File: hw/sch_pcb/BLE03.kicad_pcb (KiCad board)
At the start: 2 copper layers, 40 parts, among them J2 3.3-5V, J3 JUMP_5X2, J4 Conn_Coaxial, J5 HEADER_2x06_PARALLEL, M1 HOLE, M2 HOLE, M3 HOLE, M4 HOLE, U2 TXS0104EPW, U3 TXS0104EPW, U4 MIC5504-1.8YM5, U5 TXS0108EPW, U6 LFB212G45CG1C187, Y2 LFSPXO009682

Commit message: Adding connectors and other components
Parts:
- removed C15: 10pF, Capacitor_SMD:C_0603_1608Metric
- removed R4: 2k2, Resistor_SMD:R_0603_1608Metric
- removed R5: 10k, Resistor_SMD:R_0603_1608Metric
- removed U5: TXS0108EPW, Package_SO:TSSOP-20_4.4x6.5mm_P0.65mm
- removed U6: LFB212G45CG1C187, MLAB_SAW:Murata_C187
- added FL1: DEA162450BT-1295A, Filter_custom:RF_1260B3_TDK, F.Cu at (120.9, 76.5)
- added J1: 3V3, Mlab_Pin_Headers:Straight_2x03, F.Cu at (117.8, 82.5)
- added L1: DNP, Inductor_SMD:L_0603_1608Metric, F.Cu at (116.9, 69.4)
- added L2: DNP, Inductor_SMD:L_0603_1608Metric, F.Cu at (116.9, 71.9)
- added SW1: SW_Push, Button_Switch_THT:SW_PUSH_6mm, F.Cu at (114.3, 96.4)
- added U1: MIC5504-1.8YM5, Package_TO_SOT_SMD:SOT-23-5, F.Cu at (117.2, 89.3)
- added Y1: ABM8AIG-40.000MHZ-12-2Z-T3, Crystal:Crystal_SMD_Abracon_ABM8AIG-4Pin_3.2x2.5mm, F.Cu at (109.5, 88.1)
- C1: value 0.1uF -> 10uF; moved to F.Cu
- C10: value 6.8pF -> 1.0uF; moved to F.Cu
- C11: value 10uF -> 1.0uF; moved to F.Cu
- C12: value 100nF -> 1.0uF; moved to F.Cu
- C13: value 100nF -> 4pF; moved to F.Cu
- C14: value 1uF -> 4pF; footprint Mlab_R:SMD-0603 -> Capacitor_SMD:C_0603_1608Metric; moved to F.Cu
- C2: value 0.1uF -> 100nF; moved to F.Cu
- C3: value 0.1uF -> 1uF; footprint Capacitor_SMD:C_0603_1608Metric -> Mlab_R:SMD-0603; moved to F.Cu
- C4, C5, FID1, FID2, FID3, R2, R3, U3: moved to F.Cu
- C6, C7, C8: value 1.0uF -> 0.1uF; moved to F.Cu
- C9: value 6.8pF -> 10pF; moved to F.Cu
- D1: value LED -> BZX585-B5V6.115; footprint LED_SMD:LED_0805_2012Metric -> Diode_SMD:D_SOD-523; moved to F.Cu
- D2: value BZX585-B5V6.115 -> LED; footprint Diode_SMD:D_SOD-523 -> LED_SMD:LED_0805_2012Metric; moved to F.Cu
- J2: value 3.3-5V -> Conn_Coaxial; footprint Mlab_Pin_Headers:Straight_2x03 -> Mlab_CON:MCX; moved to F.Cu
- J3: value JUMP_5X2 -> HEADER_2x08_PARALLEL; footprint Mlab_Pin_Headers:Straight_2x04 -> Mlab_Pin_Headers:Straight_2x08
- J4: value Conn_Coaxial -> HEADER_2x05; footprint Mlab_CON:MCX -> Mlab_Pin_Headers:Straight_2x05
- J5: value HEADER_2x06_PARALLEL -> HEADER_2x08_PARALLEL; footprint Mlab_Pin_Headers:Straight_2x06 -> Mlab_Pin_Headers:Straight_2x08
- R1: value 150 -> 2k2; moved to F.Cu
- TP1: footprint TestPoint:TestPoint_Pad_D1.0mm -> TestPoint:TestPoint_Pad_D1.5mm; moved to F.Cu
- U2: value TXS0104EPW -> CC3301; footprint Package_SO:TSSOP-14_4.4x5mm_P0.65mm -> WQFN:WQFN_JARSBR_TEX; moved to F.Cu
- U4: value MIC5504-1.8YM5 -> TXS0108EPW; footprint Package_TO_SOT_SMD:SOT-23-5 -> Package_SO:TSSOP-20_4.4x6.5mm_P0.65mm; moved to F.Cu
- Y2: footprint Oscillator:Oscillator_SMD_SeikoEpson_SG210-4Pin_2.5x2.0mm -> Oscillator:Oscillator_SMD_Abracon_ASCO-4Pin_1.6x1.2mm; moved to F.Cu
- moved J3 70.5 mm to (95.5, 108.7)
- moved C1 63.0 mm to (108.9, 64.3)
- moved C13 63.0 mm to (116.9, 64.3)
- moved U2 61.2 mm to (110.8, 82.0)
- moved C7 60.7 mm to (112.9, 64.3)
- moved C14 58.8 mm to (116.9, 66.8)
- moved C11 58.7 mm to (112.9, 74.4)
- moved C2 58.3 mm to (108.9, 66.8)
- moved C8 56.0 mm to (112.9, 66.8)
- moved C12 54.6 mm to (112.9, 76.9)
- moved C3 53.7 mm to (108.9, 69.4)
- moved C6 53.3 mm to (108.9, 76.9)
- moved J2 51.5 mm to (123.3, 67.5)
- moved C9 51.4 mm to (112.9, 69.4)
- moved D2 49.4 mm to (121.2, 73.4)
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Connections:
- C1 pad 1: +1V8 -> +3V3
- C10 pad 1: Net-(U1-HFXT_M) -> +3.3V
- C11 pad 1: VCC -> Net-(U2-PA_LDO_OUT)
- C12 pad 1: VCC -> Net-(U2-DIG_LDO_OUT)
- C13 pad 1: +1V8 -> Net-(U2-HFXT_P)
- C14 pad 1: +1V8 -> Net-(U2-HFXT_M)
- C2 pad 1: +1V8 -> +3V3
- C6 pad 1: +3.3V -> +1V8
- C7 pad 1: Net-(U1-PA_LDO_OUT) -> +1V8
- C8 pad 1: Net-(U1-DIG_LDO_OUT) -> +1V8
- C9 pad 1: Net-(C9-Pad1) -> Net-(FL1-OUT)
- C9 pad 2: GND -> Net-(J2-In)
- D1 pad 1: GND -> +3V3
- D1 pad 2: Net-(D1-A) -> GND
- D2 pad 1: VCC -> GND
- D2 pad 2: GND -> Net-(D2-A)
- J2 pad 1: GND -> Net-(J2-In)
- J3 pad 1: Net-(U3-B4) -> +3V3
- J3 pad 2: Net-(U3-B4) -> +3V3
- J3 pad 3: Net-(U3-B3) -> /Connectors/SDIO_CMD_3V3
- J3 pad 4: Net-(U3-B3) -> /Connectors/SDIO_CMD_3V3
- J3 pad 5: Net-(U3-B2) -> /Connectors/SDIO_CLK_3V3
- J3 pad 6: Net-(U3-B2) -> /Connectors/SDIO_CLK_3V3
- J3 pad 7: Net-(U3-B1) -> /Connectors/SDIO_D3_3V3
- J3 pad 8: Net-(U3-B1) -> /Connectors/SDIO_D3_3V3
- J4 pad 1: Net-(J4-In) -> +1V8
- J4 pad 2: GND -> SWDIO
- J5 pad 1: GND -> +3V3
- J5 pad 10: Net-(U2-B1) -> /Connectors/UART_RX_3V3
- J5 pad 11: Net-(J5-Pad11) -> /Connectors/HOST_IRQ_WIFI_3V3
- J5 pad 12: Net-(J5-Pad11) -> /Connectors/HOST_IRQ_WIFI_3V3
- J5 pad 2: GND -> +3V3
- J5 pad 3: Net-(U2-B4) -> /Connectors/UART_RTS_3V3
- J5 pad 4: Net-(U2-B4) -> /Connectors/UART_RTS_3V3
- J5 pad 5: Net-(U2-B3) -> /Connectors/UART_CTS_3V3
- J5 pad 6: Net-(U2-B3) -> /Connectors/UART_CTS_3V3
- J5 pad 7: Net-(U2-B2) -> /Connectors/UART_TX_3V3
- J5 pad 8: Net-(U2-B2) -> /Connectors/UART_TX_3V3
- J5 pad 9: Net-(U2-B1) -> /Connectors/UART_RX_3V3
- R1 pad 1: Net-(U1-HFXT_P) -> +3V3
- R1 pad 2: Net-(C9-Pad1) -> Net-(D2-A)
- R2 pad 2: Net-(U2-OE) -> Net-(U4-OE)
- TP1 pad 1: Net-(U1-LOGGER) -> Net-(U2-LOGGER)
- U2 pad 1: +1V8 -> Net-(U2-PA_LDO_OUT)
- U2 pad 10: Net-(U2-B4) -> unconnected-(U2-COEX_REQ-Pad10)
- U2 pad 11: Net-(U2-B3) -> UART_RTS
- U2 pad 12: Net-(U2-B2) -> UART_CTS
- U2 pad 13: Net-(U2-B1) -> UART_TX
- U2 pad 14: VCC -> UART_RX
- U2 pad 2: SWCLK -> /RF_BG
- U2 pad 3: SWDIO -> GND
- U2 pad 4: NRESET -> +1V8
- U2 pad 5: unconnected-(U2-A4-Pad5) -> +1V8
- U2 pad 6: unconnected-(U2-NC-Pad6) -> Net-(U2-HFXT_P)
- U2 pad 7: GND -> Net-(U2-HFXT_M)
- U2 pad 8: Net-(U2-OE) -> unconnected-(U2-COEX_GRANT-Pad8)
- U3 pad 1: +1V8 -> +3V3
- U3 pad 10: Net-(U3-B4) -> HOST_IRQ_BLE
- U3 pad 11: Net-(U3-B3) -> HOST_IRQ_WIFI
- U3 pad 12: Net-(U3-B2) -> SDIO_D0
- U3 pad 13: Net-(U3-B1) -> SDIO_D1
- U3 pad 14: VCC -> +1V8
- U3 pad 2: UART_RX -> /Connectors/SDIO_D1_3V3
- U3 pad 3: UART_TX -> /Connectors/SDIO_D0_3V3
- U3 pad 4: UART_CTS -> /Connectors/HOST_IRQ_WIFI_3V3
- U3 pad 5: UART_RTS -> /Connectors/HOST_IRQ_BLE_3V3
- U4 pad 1: VCC -> /Connectors/UART_RTS_3V3
- U4 pad 2: GND -> +3V3
- U4 pad 3: VCC -> /Connectors/UART_CTS_3V3
- U4 pad 4: unconnected-(U4-NC-Pad4) -> /Connectors/UART_TX_3V3
- U4 pad 5: +1V8 -> /Connectors/UART_RX_3V3
- Y2 pad 1: +1V8 -> unconnected-(Y2-Tri-State-Pad1)

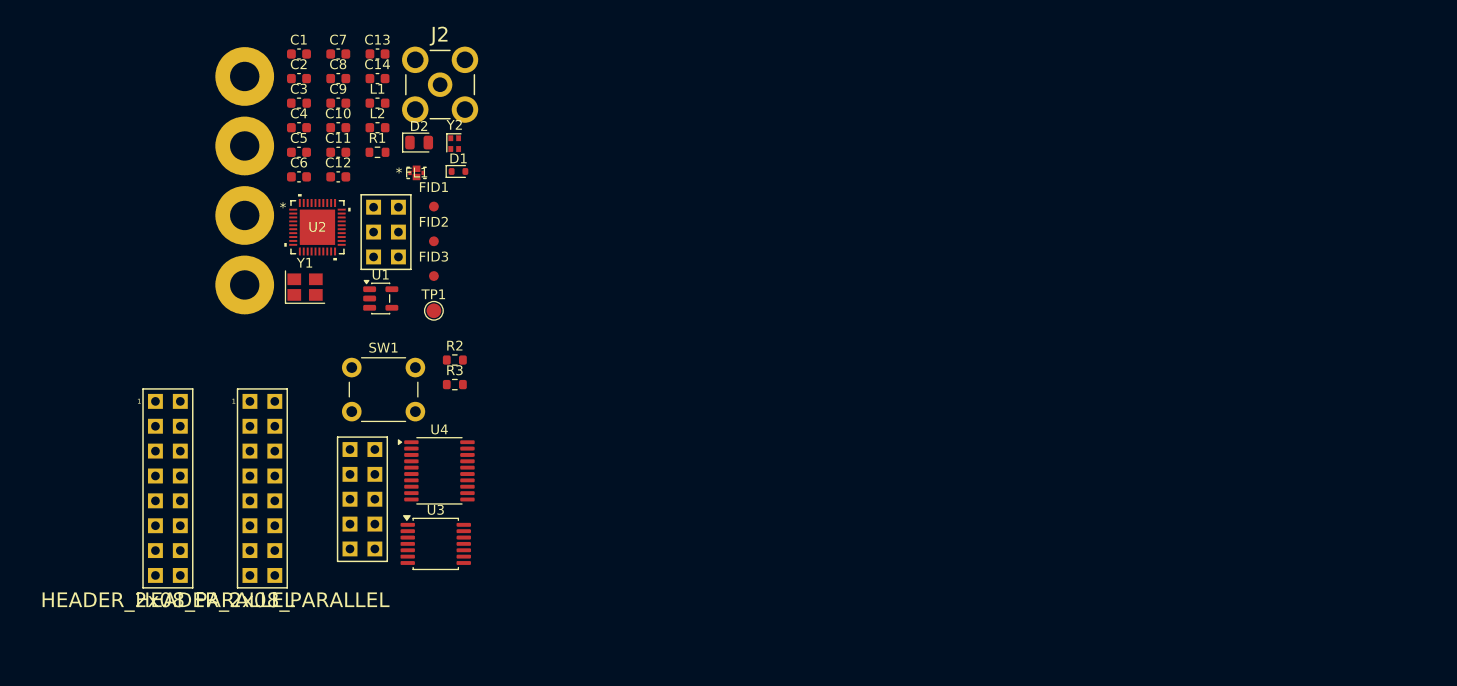
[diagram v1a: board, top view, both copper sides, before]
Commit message: Improving sch and adding RC filter for reset line
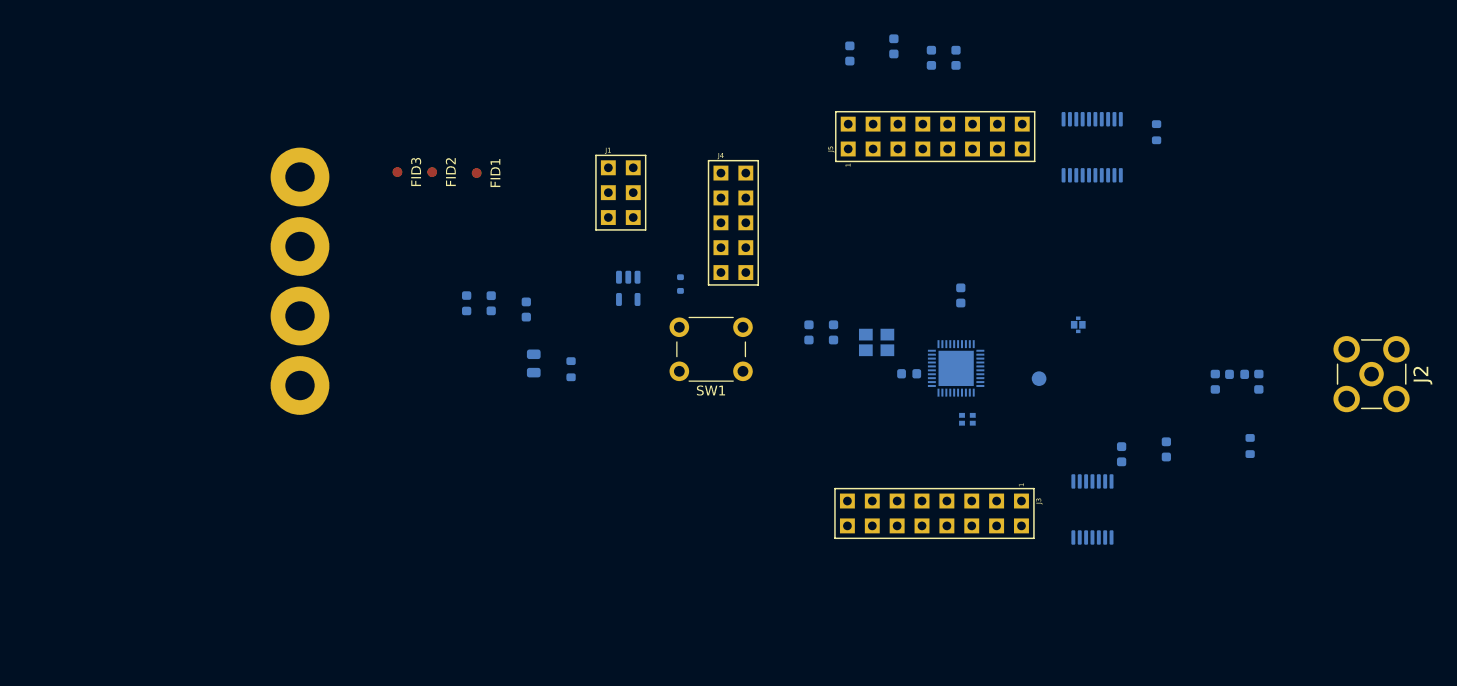
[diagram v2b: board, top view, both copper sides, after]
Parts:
- C1, C10, C11, C12, C2, C3, C4, C5, C6, C7, C8, C9, D1, D2, FL1, L1, L2, R1, R2, R3, TP1, U1, U2, U3, U4, Y1, Y2: moved to B.Cu
- C13, C14: value 4pF -> 16pF; moved to B.Cu
- moved J2 99.6 mm to (218.5, 97.0), turned to -90 degrees
- moved C9 95.9 mm to (204.7, 97.1), turned to 180 degrees
- moved L1 94.4 mm to (206.9, 97.8), turned to 90 degrees
- moved C5 93.7 mm to (197.5, 104.7), turned to 90 degrees
- moved L2 89.4 mm to (202.5, 97.8), turned to -90 degrees
- moved C6 88.7 mm to (192.9, 105.2), turned to 90 degrees
- moved R3 81.5 mm to (206.1, 104.4), turned to 90 degrees
- moved J3 78.3 mm to (173.8, 111.3), turned to -90 degrees
- moved J5 77.6 mm to (173.9, 72.8), turned to 90 degrees
- moved R2 75.4 mm to (196.5, 72.3), turned to 90 degrees
- moved U4 74.4 mm to (189.9, 73.9), turned to -90 degrees
- moved C4 69.7 mm to (176.5, 89.0), turned to 90 degrees
- moved FL1 69.4 mm to (188.5, 92.0), turned to 90 degrees
- moved U3 67.2 mm to (189.9, 110.9), turned to 90 degrees
- moved C7 66.8 mm to (171.2, 97.0), turned to 180 degrees
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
